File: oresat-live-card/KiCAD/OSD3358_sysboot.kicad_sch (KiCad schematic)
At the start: 11 parts, among them U7 OSD3358-512M-BSM

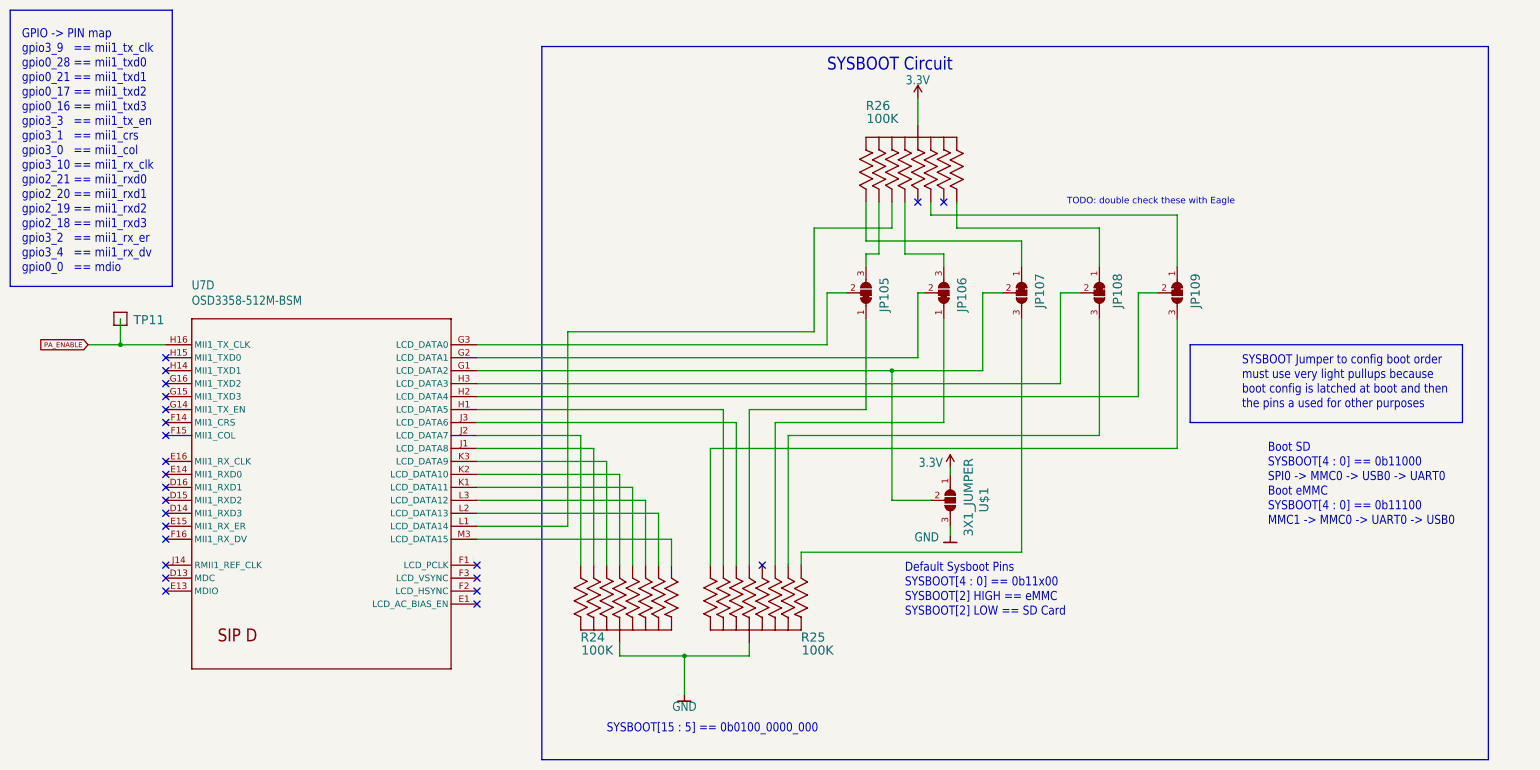
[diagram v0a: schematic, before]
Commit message: Updated OreSat Live Card. Added changes from the C3 v6 Octavo circuitry and GPS card update. Fixed some GitHub issues. Board layout still in progress.
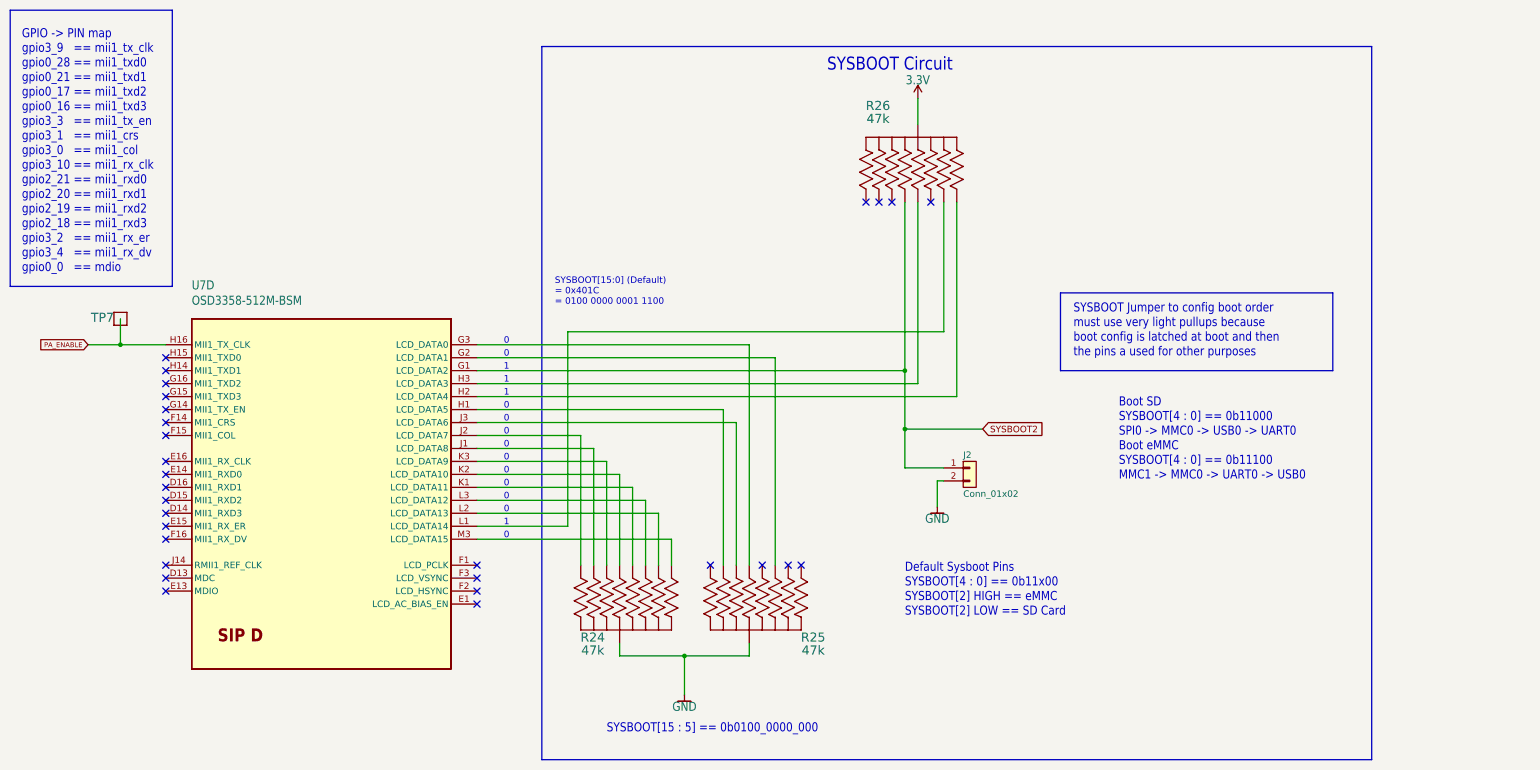
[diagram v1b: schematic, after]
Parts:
- removed JP105, JP106, JP107, JP108, JP109: JUMPER-SMT_3_1-NC_TRACE_SILK, oresat-live-card:SMT-JUMPER_3_1-NC_TRACE_SILK, symbol Jumper:SolderJumper_3_Bridged12
- removed TP11: TEST-POINT, oresat-live-card:PAD.03X.04, symbol oresat-live-card-eagle-import:TEST-POINT
- removed U$1: 3X1_JUMPER, Jumper:SolderJumper-3_P1.3mm_Open_RoundedPad1.0x1.5mm_NumberLabels, symbol Jumper:SolderJumper_3_Open
- added J2: Conn_01x02, Connector_PinHeader_2.54mm:PinHeader_1x02_P2.54mm_Vertical, symbol Connector_Generic:Conn_01x02
- added TP7: TEST-POINT3X4, oresat-misc:TestPoint_Pad_D1.0mm, symbol oresat-misc:Test-Point-1mm-round
- R24, R25, R26: symbol oresat-live-card-eagle-import:EXB-A10P391JC_ARRAY_EXBA-M -> oresat-passives:EXB-A10P391J
- U7: footprint oresat-live-card:OSD335X-BGA-256 -> oresat-ics:U-Octavo-OSD335X-BGA-256; symbol oresat-live-card-eagle-import:OSD3358-512M-BSM -> oresat-ics:OSD3358-512M-BSM
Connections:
- net GND: now also J2.2 (Pin_2)
- net PA_ENABLE: now also TP7.1
- net at R26.6 (66): now also U7.H2 (LCD_DATA4)
- net at U7.H3 (LCD_DATA3): now also R26.3 (33)
- net at R26.2 (22): no longer U7.L1 (LCD_DATA14)
- net at R26.4 (44): now also U7.L1 (LCD_DATA14)
- net SYSBOOT2: now reaches R26.8 (88)
- net SYSBOOT2: now also U7.G1 (LCD_DATA2), J2.1 (Pin_1)
- net at U7.G2 (LCD_DATA1): now also R25.2 (22)
- net at U7.G3 (LCD_DATA0): now also R25.3 (33)
- no-connect marks 24 -> 29
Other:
- note added: "0"
- note added: "1"
- note added: "SYSBOOT[15:0] (Default) = 0x401C = 0100 0000 0001 1100"
- note removed: "TODO: double check these with Eagle"

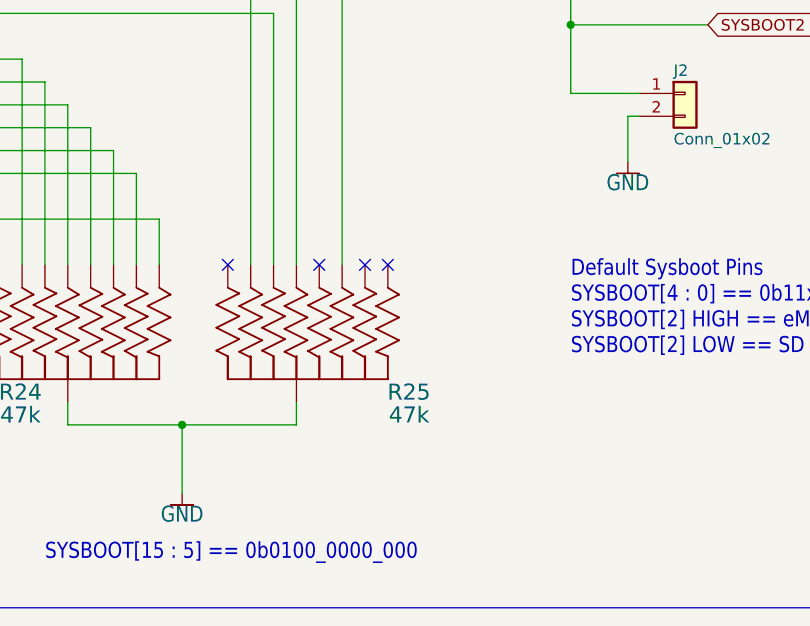
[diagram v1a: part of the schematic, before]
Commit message: Cleaned up ERC and DRC errors on DxWiFi Card
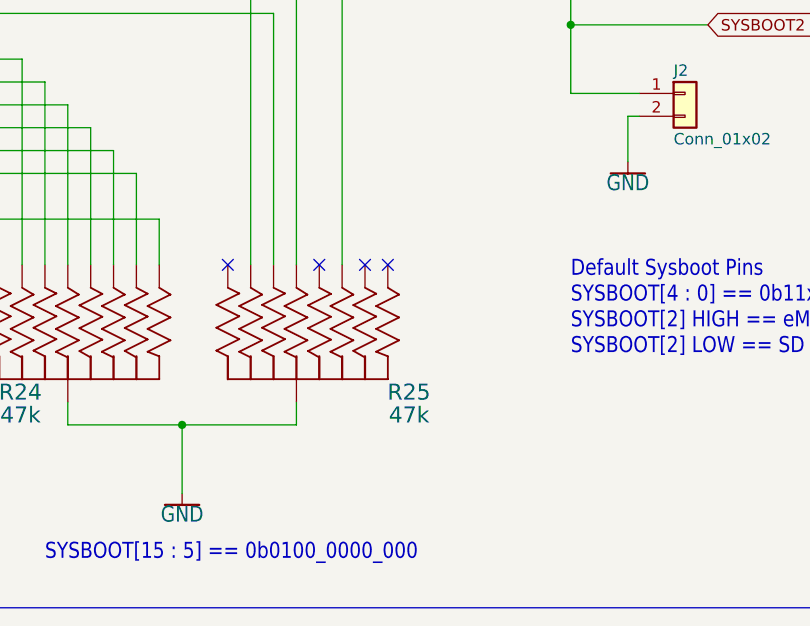
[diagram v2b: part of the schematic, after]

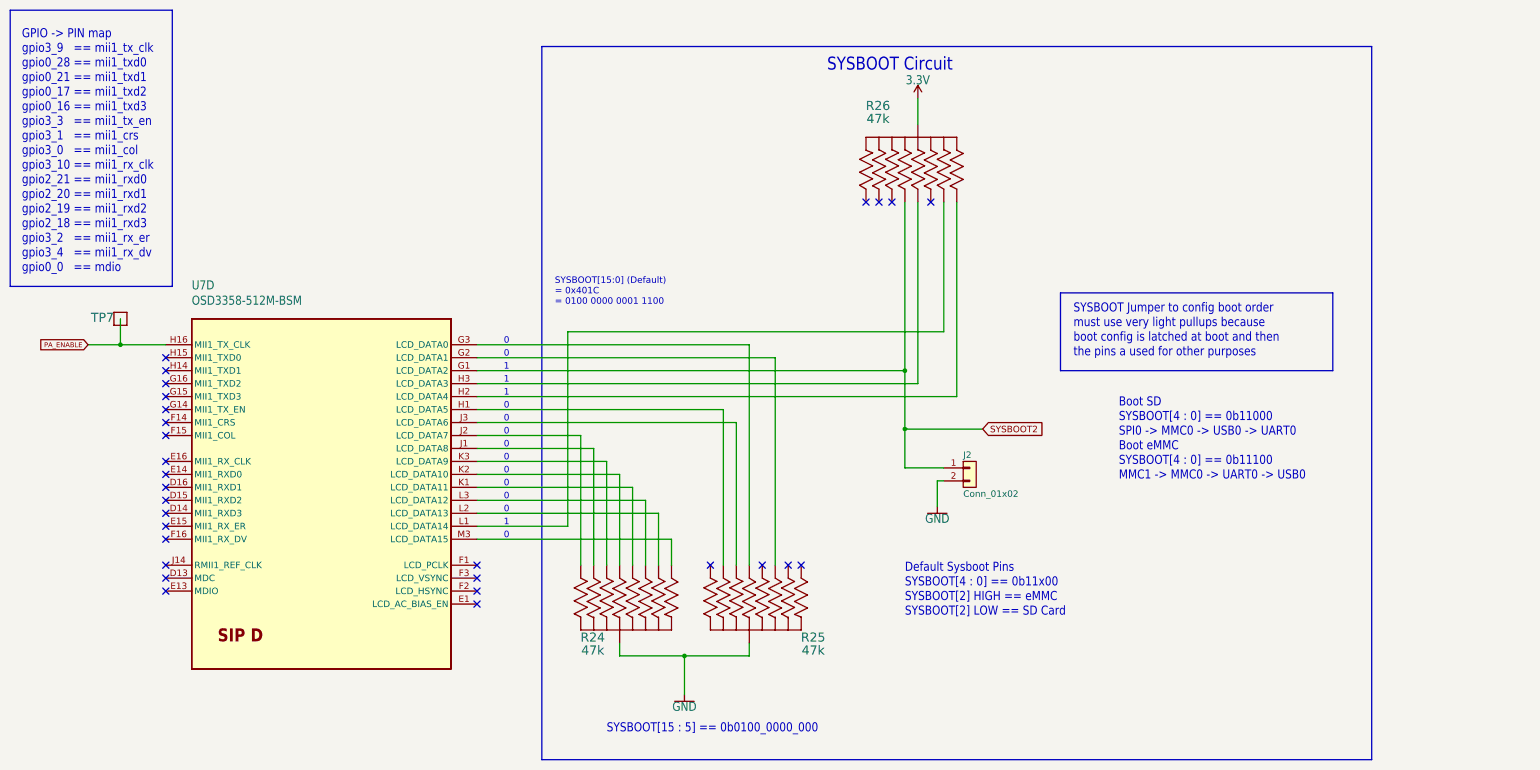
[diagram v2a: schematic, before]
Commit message: Upgraded to KiCAD 8.0. Added notes on U.FL cable and USB cables to wifi and camera.
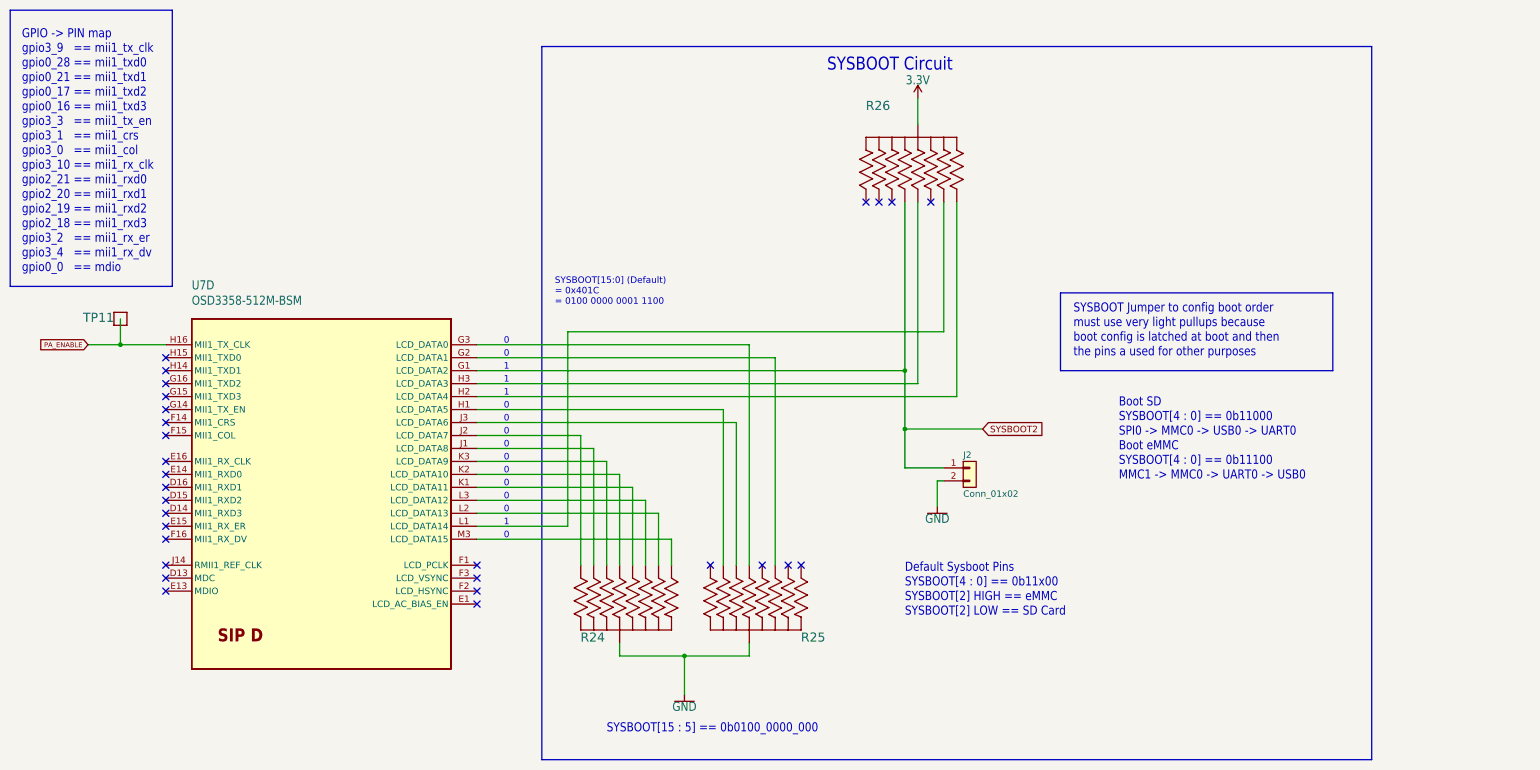
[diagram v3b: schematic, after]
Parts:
- renumbered TP7 to TP11

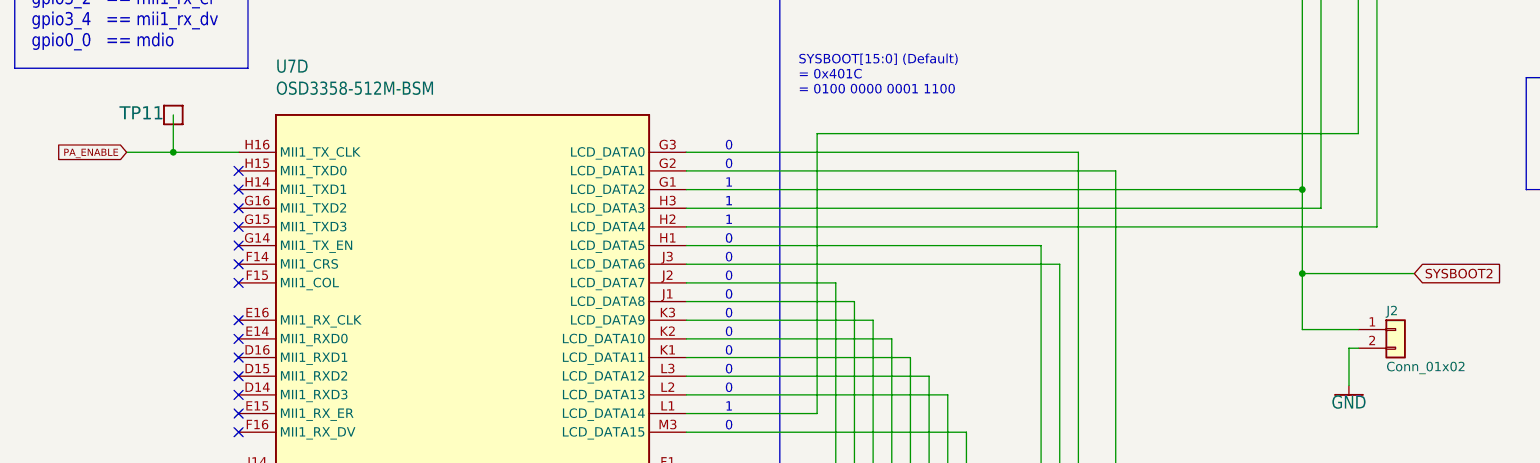
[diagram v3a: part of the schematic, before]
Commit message: added new sheets for LNA and switching
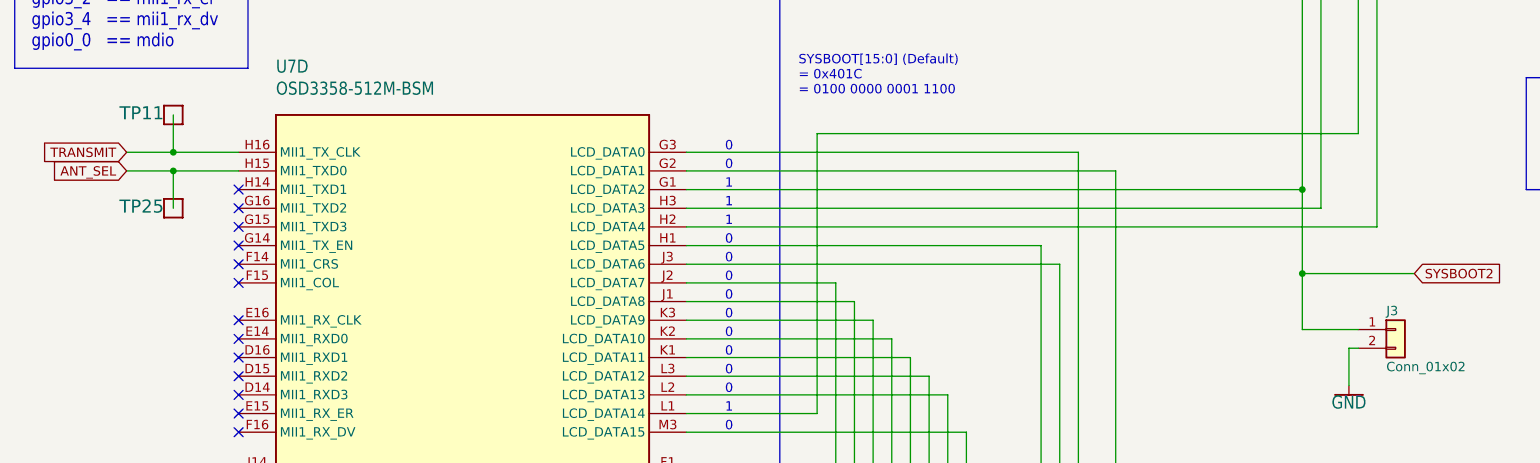
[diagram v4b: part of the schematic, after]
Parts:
- added TP25: TEST-POINT3X4, oresat-misc:TestPoint_Pad_D1.0mm, symbol oresat-misc:Test-Point-1mm-round
- renumbered J2 to J3
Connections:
- net ANT_SEL: now reaches U7.H15 (MII1_TXD0)
- net ANT_SEL: now also TP25.1
- net PA_ENABLE renamed TRANSMIT
- no-connect marks 29 -> 28
